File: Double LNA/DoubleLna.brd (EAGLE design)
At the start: 176.5 x 101.3 mm, 33 parts, among them IC1 TP4056, J1 DCJ0202

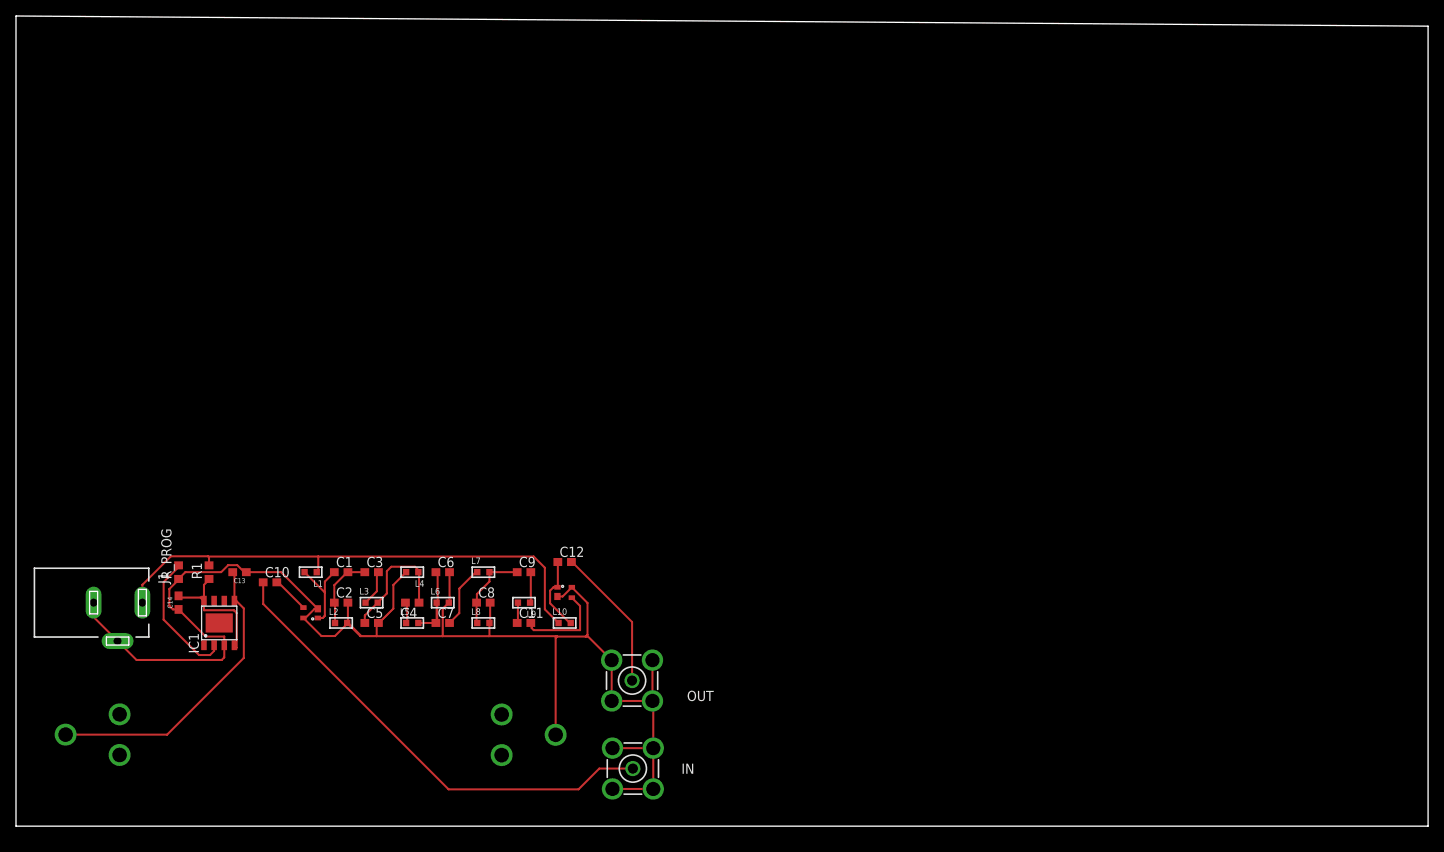
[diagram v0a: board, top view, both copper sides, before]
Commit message: added uass ground station
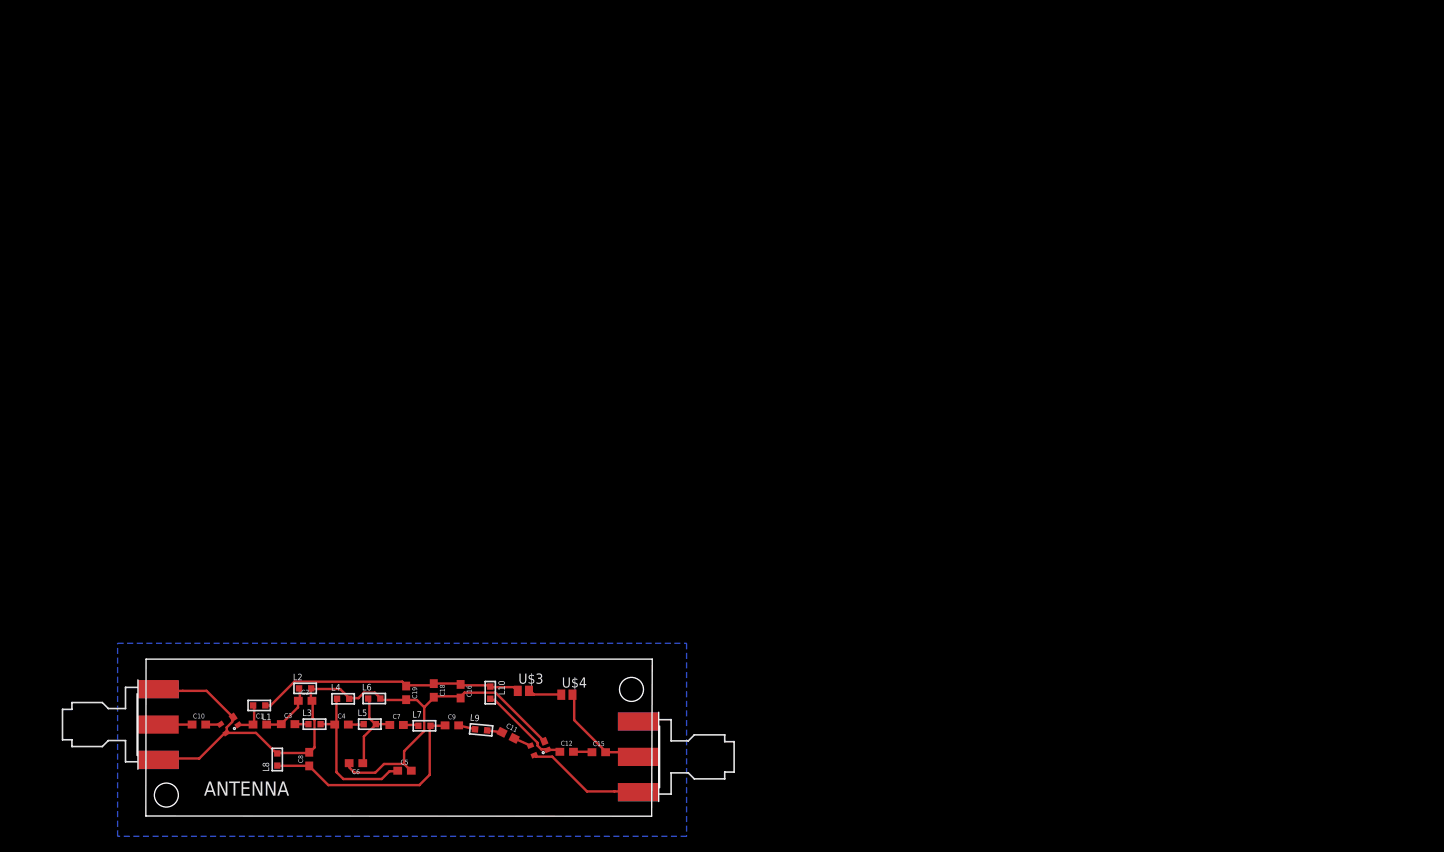
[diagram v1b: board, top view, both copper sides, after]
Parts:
- removed BT1: (no value), SparkFun-Batteries:BATTERY_18650-HOLDER
- removed C13, C14: 10uf, SparkFun-Capacitors:0603
- removed IC1: TP4056, TP4056:SOP-8
- removed IN, OUT: BU-SMA-V, con-coax:BU-SMA-V
- removed J1: DCJ0202, con-jack:DCJ0202
- removed R1: .4ohm, adafruit:R0603
- removed R_PROG: 10k, adafruit:R0603
- added ANTENNA, X2: SMA-142-0701-871/876, con-coax:J502-ND-142-0701-871/876
- added C15: 10uH, SparkFun-Capacitors:0603
- added C16: 100pf, SparkFun-Capacitors:0603
- added C18: 1nf, SparkFun-Capacitors:0603
- added C19: 10nf, SparkFun-Capacitors:0603
- added U$3, U$4: 1.5uH, rcl-2:C0504
- moved L8 30.9 mm to (16.2, 8.33), turned to 90 degrees
- moved C8 29.3 mm to (20.1, 8.38), turned to 90 degrees
- moved C6 26.2 mm to (26.0, 7.87), turned to 180 degrees
- moved C12 23.7 mm to (52.3, 9.30)
- moved C3 21.7 mm to (17.5, 12.8)
- moved C1 21.6 mm to (14.0, 12.7)
- moved C9 21.2 mm to (38.0, 12.6)
- moved L7 20.6 mm to (34.5, 12.5)
- moved C10 19.9 mm to (6.35, 12.7)
- moved U$2 19.7 mm to (48.9, 9.80), turned to 112 degrees
- moved C5 18.9 mm to (32.1, 6.93)
- moved L4 18.0 mm to (24.4, 15.9), turned to 0 degrees
- moved L1 17.9 mm to (13.9, 15.1)
- moved C4 17.6 mm to (24.2, 12.7), turned to 0 degrees
- moved U$1 17.3 mm to (10.2, 12.7), turned to 123.7 degrees
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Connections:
- removed net N$17: BT1.PWR@1, C13.2, IC1.5
- removed net N$18: IC1.2, R_PROG.2
- removed net N$19: C14.2, IC1.4, IC1.8, R1.1
- removed net RAW_VCC: J1.1, L1.1, L10.1, R1.2
- new net N$21: C15.2, U$4.2, X2.1
- new net N$22: U$3.2, U$4.1
- new net VCC: C16.1, C18.1, C19.1, L1.1, L10.1, U$3.1
- net GND: now also ANTENNA.G@1, ANTENNA.G@2, ANTENNA.G@3, ANTENNA.G@4, C16.2, C18.2, C19.2, X2.G@1, X2.G@2, X2.G@3, X2.G@4; no longer BT1.GND@1, C13.1, C14.1, IC1.3, IN.2, IN.3, IN.4, IN.5, J1.2, J1.3, OUT.2, OUT.3, OUT.4, OUT.5, R_PROG.1
- net N$1: now also ANTENNA.1; no longer IN.1
- net N$14: now also C15.1; no longer OUT.1
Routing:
- net GND: track 195.6 -> 109.9 mm
- net RAW_VCC: track 65.5 -> 0.00 mm
- net N$1: track 59.6 -> 4.20 mm
- net N$17: track 37.7 -> 0.00 mm
- net VCC: track 0.00 -> 33.7 mm
- net N$19: track 31.0 -> 0.00 mm
- net N$8: track 10.8 -> 28.6 mm
- net N$18: track 16.7 -> 0.00 mm
- net N$14: track 18.0 -> 2.33 mm
- net N$21: track 0.00 -> 13.2 mm
- net N$13: track 11.4 -> 2.22 mm
- net N$11: track 10.6 -> 4.45 mm
- net N$7: track 7.90 -> 1.91 mm
- net N$22: track 0.00 -> 4.23 mm
- net N$4: track 16.1 -> 19.7 mm
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- added copper zone on layer 16, net GND
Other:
- board size 176.5 x 101.3 mm -> 63.3 x 19.6 mm
